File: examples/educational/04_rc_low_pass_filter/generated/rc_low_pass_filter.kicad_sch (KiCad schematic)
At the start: 4 parts

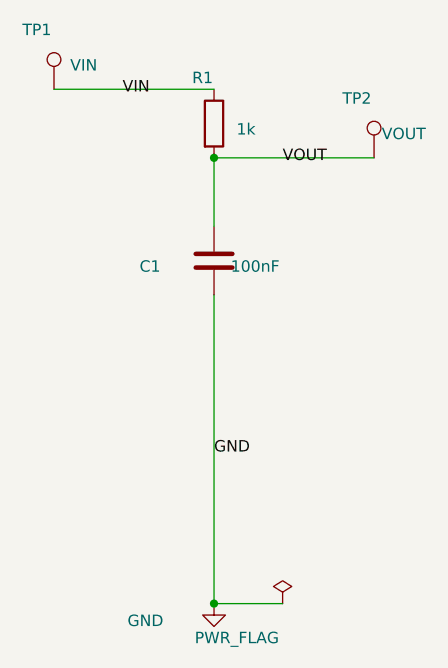
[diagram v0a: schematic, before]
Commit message: feat: infer conventional schematic topology layouts
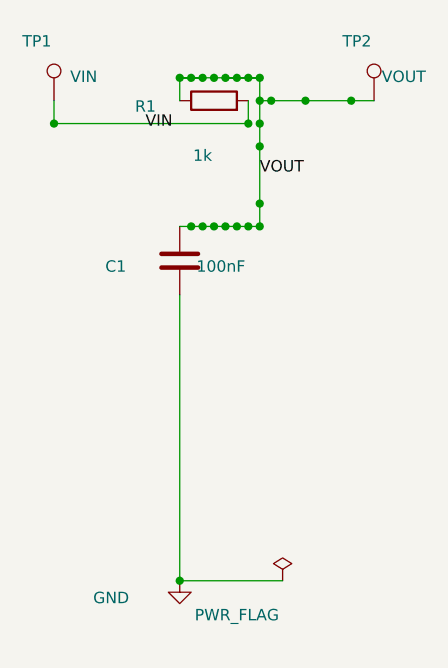
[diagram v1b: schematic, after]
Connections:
- net VIN: now also R1.2; no longer R1.1
- net VOUT: now also R1.1; no longer R1.2
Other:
- moved on the sheet: C1, R1, TP1, TP2
